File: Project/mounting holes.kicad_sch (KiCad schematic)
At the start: 26 parts

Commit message: plate work
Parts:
- removed H19, H20, H26: MountingHole, cipulot_parts:HOLE_M2, symbol Mechanical:MountingHole
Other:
- moved on the sheet: H21, H22, H23, H24, H25

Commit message: pcb & plate revisions & firmware
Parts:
- added H25 (x2): MountingHole, cipulot_parts:HOLE_M2, symbol Mechanical:MountingHole
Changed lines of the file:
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@@
+    )
+  )
+  (symbol (lib_id "Mechanical:MountingHole") (at 51.435 121.92 0) (unit 1)
+    (in_bom yes) (on_board yes) (dnp no) (fields_autoplaced)
+    (property "Reference" "H25" (at 53.975 121.0853 0)
+      (effects (font (size 1.27 1.27)) (justify left))
+    )
+    (property "Value" "MountingHole" (at 53.975 123.6222 0)
+      (effects (font (size 1.27 1.27)) (justify left))
+    )
+    (property "Footprint" "cipulot_parts:HOLE_M2" (at 51.435 121.92 0)
+      (effects (font (size 1.27 1.27)) hide)
+    )
+    (property "Datasheet" "~" (at 51.435 121.92 0)
+      (effects (font (size 1.27 1.27)) hide)
+    )
+    (instances
+      (project "the-nicholas-van"
+        (path "/38f182bd-9097-4ce3-95d4-cd91b210c79b"
+          (reference "H25") (unit 1)
+        )
+        (path "/38f182bd-9097-4ce3-95d4-cd91b210c79b/610cabd0-87c8-472b-8f6a-63e84b5c9031"
+          (reference "H25") (unit 1)
+        )
+      )
+      (project "mounting holes"
+        (path "/5a4b5506-e3f1-48e7-9020-bb3c3e3fc15f"
+          (reference "H25") (unit 1)
+        )
+      )
+      (project "travaulta"
+        (path "/690df46b-b605-4617-b545-6aaced86d0fc/794114ef-7db2-4f90-86d0-13c32bb11aa3"
+          (reference "H8") (unit 1)
+        )
+      )
+      (project "EC60"
+        (path "/e63e39d7-6ac0-4ffd-8aa3-1841a4541b55/004107b0-ccf4-476d-9504-97bf1a9256af"
+          (reference "H1") (unit 1)
+        )
+      )
+      (project "ampersand"
+        (path "/e827c860-43eb-4910-9ede-2f2080093daa/529a754c-c9af-494c-aed5-3f327fcdc592"
+          (reference "H19") (unit 1)
+        )
+      )
+      (project "forti EC"
+        (path "/f5e5948c-eeca-4160-a5f8-686f765d01ce/55e2d8c6-9092-40f0-965e-73dea8a35aef"
+          (reference "H25") (unit 1)
+        )
+      )
     )
   )
@@
         )
       )
+    )
+  )
+  (symbol (lib_id "Mechanical:MountingHole") (at 76.835 122.555 0) (unit 1)
+    (in_bom yes) (on_board yes) (dnp no) (fields_autoplaced)
+    (property "Reference" "H25" (at 79.375 121.7203 0)
+      (effects (font (size 1.27 1.27)) (justify left))
+    )
+    (property "Value" "MountingHole" (at 79.375 124.2572 0)
+      (effects (font (size 1.27 1.27)) (justify left))
+    )
+    (property "Footprint" "cipulot_parts:HOLE_M2" (at 76.835 122.555 0)
+      (effects (font (size 1.27 1.27)) hide)
+    )
+    (property "Datasheet" "~" (at 76.835 122.555 0)
+      (effects (font (size 1.27 1.27)) hide)
+    )
+    (instances
+      (project "the-nicholas-van"
+        (path "/38f182bd-9097-4ce3-95d4-cd91b210c79b"
+          (reference "H25") (unit 1)
+        )
+        (path "/38f182bd-9097-4ce3-95d4-cd91b210c79b/610cabd0-87c8-472b-8f6a-63e84b5c9031"
+          (reference "H25") (unit 1)
+        )
+      )
+      (project "mounting holes"
+        (path "/5a4b5506-e3f1-48e7-9020-bb3c3e3fc15f"
+          (reference "H25") (unit 1)
+        )
+      )
+      (project "travaulta"
+        (path "/690df46b-b605-4617-b545-6aaced86d0fc/794114ef-7db2-4f90-86d0-13c32bb11aa3"
+          (reference "H8") (unit 1)
+        )
+      )
+      (project "EC60"
+        (path "/e63e39d7-6ac0-4ffd-8aa3-1841a4541b55/004107b0-ccf4-476d-9504-97bf1a9256af"
+          (reference "H1") (unit 1)
+        )
+      )
+      (project "ampersand"
+        (path "/e827c860-43eb-4910-9ede-2f2080093daa/529a754c-c9af-494c-aed5-3f327fcdc592"
+          (reference "H20") (unit 1)
+        )
+      )
+      (project "forti EC"
+        (path "/f5e5948c-eeca-4160-a5f8-686f765d01ce/55e2d8c6-9092-40f0-965e-73dea8a35aef"
+          (reference "H25") (unit 1)
+        )
+      )

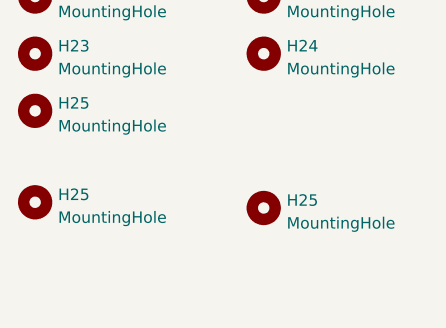
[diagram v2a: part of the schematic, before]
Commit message: bottom row change, plate update, firmware update
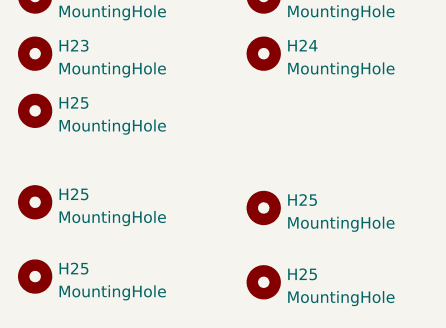
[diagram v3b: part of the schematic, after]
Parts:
- added H25 (x2): MountingHole, cipulot_parts:HOLE_M2, symbol Mechanical:MountingHole
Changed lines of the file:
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@@
+    )
+  )
+  (symbol (lib_id "Mechanical:MountingHole") (at 76.835 130.81 0) (unit 1)
+    (in_bom yes) (on_board yes) (dnp no) (fields_autoplaced)
+    (property "Reference" "H25" (at 79.375 129.9753 0)
+      (effects (font (size 1.27 1.27)) (justify left))
+    )
+    (property "Value" "MountingHole" (at 79.375 132.5122 0)
+      (effects (font (size 1.27 1.27)) (justify left))
+    )
+    (property "Footprint" "cipulot_parts:HOLE_M2" (at 76.835 130.81 0)
+      (effects (font (size 1.27 1.27)) hide)
+    )
+    (property "Datasheet" "~" (at 76.835 130.81 0)
+      (effects (font (size 1.27 1.27)) hide)
+    )
+    (instances
+      (project "the-nicholas-van"
+        (path "/38f182bd-9097-4ce3-95d4-cd91b210c79b"
+          (reference "H25") (unit 1)
+        )
+        (path "/38f182bd-9097-4ce3-95d4-cd91b210c79b/610cabd0-87c8-472b-8f6a-63e84b5c9031"
+          (reference "H25") (unit 1)
+        )
+      )
+      (project "mounting holes"
+        (path "/5a4b5506-e3f1-48e7-9020-bb3c3e3fc15f"
+          (reference "H25") (unit 1)
+        )
+      )
+      (project "travaulta"
+        (path "/690df46b-b605-4617-b545-6aaced86d0fc/794114ef-7db2-4f90-86d0-13c32bb11aa3"
+          (reference "H8") (unit 1)
+        )
+      )
+      (project "EC60"
+        (path "/e63e39d7-6ac0-4ffd-8aa3-1841a4541b55/004107b0-ccf4-476d-9504-97bf1a9256af"
+          (reference "H1") (unit 1)
+        )
+      )
+      (project "ampersand"
+        (path "/e827c860-43eb-4910-9ede-2f2080093daa/529a754c-c9af-494c-aed5-3f327fcdc592"
+          (reference "H27") (unit 1)
+        )
+      )
+      (project "forti EC"
+        (path "/f5e5948c-eeca-4160-a5f8-686f765d01ce/55e2d8c6-9092-40f0-965e-73dea8a35aef"
+          (reference "H25") (unit 1)
+        )
+      )
     )
   )
@@
         )
       )
+      (project "forti EC"
+        (path "/f5e5948c-eeca-4160-a5f8-686f765d01ce/55e2d8c6-9092-40f0-965e-73dea8a35aef"
+          (reference "H25") (unit 1)
+        )
+      )
+    )
+  )
+  (symbol (lib_id "Mechanical:MountingHole") (at 51.435 130.175 0) (unit 1)
+    (in_bom yes) (on_board yes) (dnp no) (fields_autoplaced)
+    (property "Reference" "H25" (at 53.975 129.3403 0)
+      (effects (font (size 1.27 1.27)) (justify left))
+    )
+    (property "Value" "MountingHole" (at 53.975 131.8772 0)
+      (effects (font (size 1.27 1.27)) (justify left))
+    )
+    (property "Footprint" "cipulot_parts:HOLE_M2" (at 51.435 130.175 0)
+      (effects (font (size 1.27 1.27)) hide)
+    )
+    (property "Datasheet" "~" (at 51.435 130.175 0)
+      (effects (font (size 1.27 1.27)) hide)
+    )
+    (instances
+      (project "the-nicholas-van"
+        (path "/38f182bd-9097-4ce3-95d4-cd91b210c79b"
+          (reference "H25") (unit 1)
+        )
+        (path "/38f182bd-9097-4ce3-95d4-cd91b210c79b/610cabd0-87c8-472b-8f6a-63e84b5c9031"
+          (reference "H25") (unit 1)
+        )
+      )
+      (project "mounting holes"
+        (path "/5a4b5506-e3f1-48e7-9020-bb3c3e3fc15f"
+          (reference "H25") (unit 1)
+        )
+      )
+      (project "travaulta"
+        (path "/690df46b-b605-4617-b545-6aaced86d0fc/794114ef-7db2-4f90-86d0-13c32bb11aa3"
+          (reference "H8") (unit 1)
+        )
+      )
+      (project "EC60"
+        (path "/e63e39d7-6ac0-4ffd-8aa3-1841a4541b55/004107b0-ccf4-476d-9504-97bf1a9256af"
+          (reference "H1") (unit 1)
+        )
+      )
+      (project "ampersand"
+        (path "/e827c860-43eb-4910-9ede-2f2080093daa/529a754c-c9af-494c-aed5-3f327fcdc592"
+          (reference "H26") (unit 1)
+        )
+      )

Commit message: v1 production files
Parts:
- added H28, H29: MountingHole, cipulot_parts:HOLE_M2 (no arrow), symbol Mechanical:MountingHole
- H1, H10, H11, H12, H13, H14, H15, H16, H17, H18, H2, H21, H22, H23, H24, H25, H3, H4, H5, H6, H7, H8, H9: footprint cipulot_parts:HOLE_M2 -> cipulot_parts:HOLE_M2 (no arrow)
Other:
- moved on the sheet: H1, H10, H11, H12, H13, H14, H15, H16, H17, H18, H2, H21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
